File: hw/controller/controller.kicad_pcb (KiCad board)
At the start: 2 copper layers, 76.2 x 38.1 mm, 87 parts, among them J2 USB_OTG, J3 UART, P14 I2C0, P15 I2C1, P16 I2C2, P17 I2C3, P2 FRIDGE, P3 FAN, P4 PUMP, P5 MIST, SW1 RST, SW2 BOOT, U1 stm32f072x, U2 MIC550X, U3 tca9546a, U8 SHT3x-DIS, Y2 32768Hz

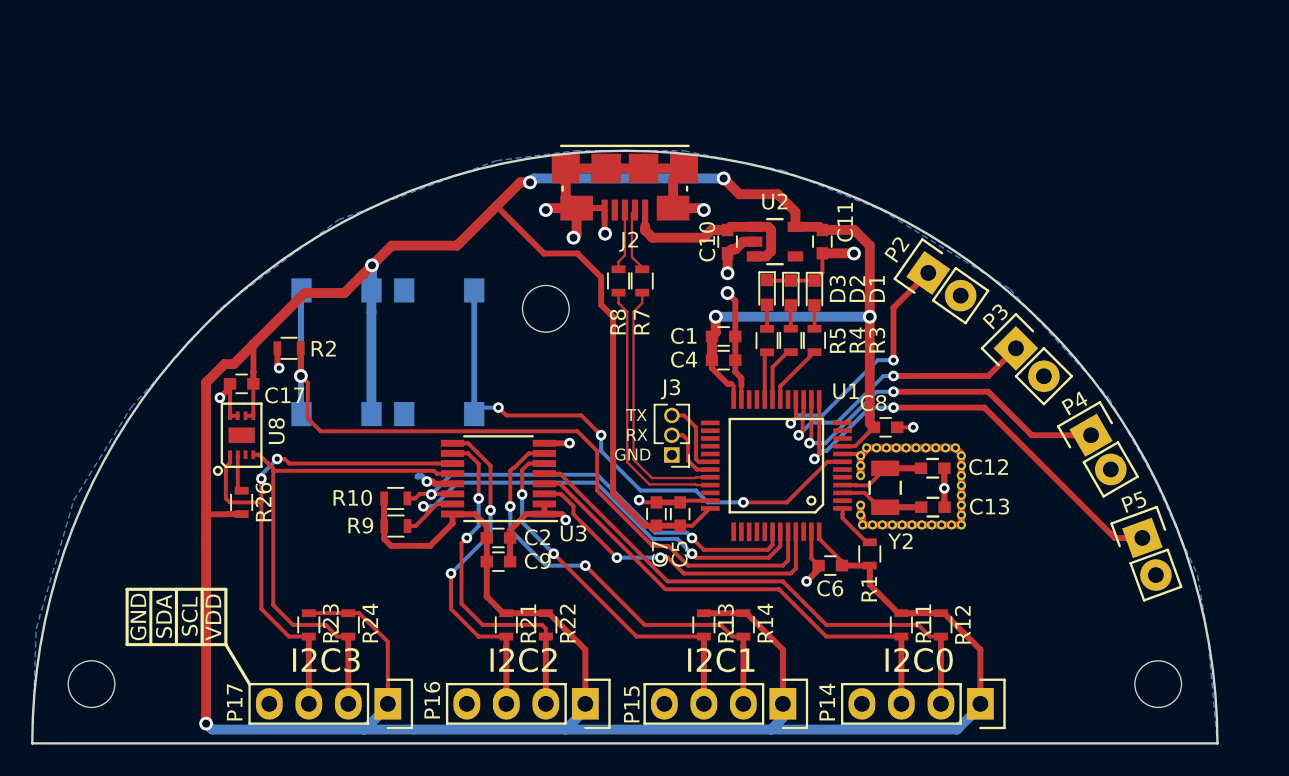
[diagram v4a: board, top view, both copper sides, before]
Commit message: Updated ostur_controller with NRF52810. Released v2.0
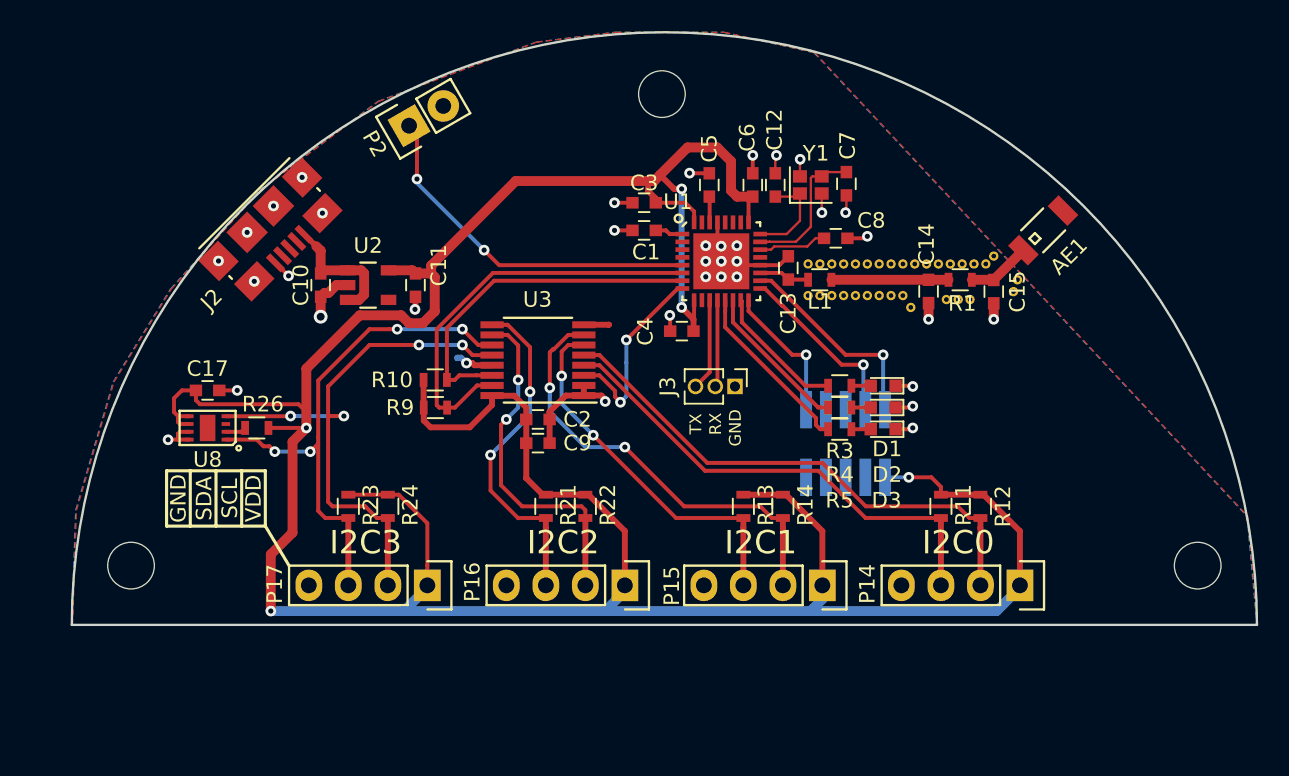
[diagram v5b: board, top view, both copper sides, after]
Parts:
- removed P3: FAN, Pin_Headers:Pin_Header_Straight_1x02
- removed P4: PUMP, Pin_Headers:Pin_Header_Straight_1x02
- removed P5: MIST, Pin_Headers:Pin_Header_Straight_1x02
- removed R2: 10k, Resistors_SMD:R_0603
- removed R7, R8: 22, Resistors_SMD:R_0603
- removed the REF** at (151.2, 96.0)
- removed the REF** at (155.8, 97.3)
- removed the REF** at (156.4, 97.3)
- removed the REF** at (157.1, 97.3)
- removed the REF** at (157.7, 97.3)
- removed the REF** at (157.7, 96.7)
- removed the REF** at (157.7, 96.0)
- removed the REF** at (157.7, 95.4)
- removed the REF** at (157.7, 94.8)
- removed the REF** at (157.7, 94.1)
- removed the REF** at (157.7, 93.5)
- removed the REF** at (151.2, 96.7)
- removed the REF** at (157.7, 92.9)
- removed the REF** at (157.3, 92.3)
- removed the REF** at (156.7, 92.3)
- removed the REF** at (156.0, 92.3)
- removed the REF** at (155.4, 92.3)
- removed the REF** at (154.8, 92.3)
- removed the REF** at (154.1, 92.3)
- removed the REF** at (153.5, 92.3)
- removed the REF** at (152.9, 92.3)
- removed the REF** at (151.6, 92.3)
- removed the REF** at (151.3, 97.3)
- removed the REF** at (151.2, 92.9)
- removed the REF** at (151.2, 93.5)
- removed the REF** at (151.2, 94.1)
- removed the REF** at (152.2, 92.3)
- removed the REF** at (152.0, 97.3)
- removed the REF** at (152.6, 97.3)
- removed the REF** at (153.2, 97.3)
- removed the REF** at (153.9, 97.3)
- removed the REF** at (154.5, 97.3)
- removed the REF** at (155.1, 97.3)
- removed SW1: RST, footprints:PTS645SM43SMTR92
- removed SW2: BOOT, footprints:PTS645SM43SMTR92
- removed Y2: 32768Hz, footprints:FC-135
- added AE1: Antenna, alvarop:AMCA31-2R450G-S1F-T3, F.Cu at (162.9, 78.4)
- added C14: DNP, Capacitors_SMD:C_0603, F.Cu at (155.6, 82.3)
- added C15: DNP, Capacitors_SMD:C_0603, F.Cu at (159.8, 82.3)
- added C3: 4.7uF, Capacitors_SMD:C_0603, F.Cu at (137.3, 76.6)
- added J1: ARM-SWD, alvarop:ARM_SWD_SMD, B.Cu at (150.2, 92.1)
- added L1: 3.9nH, Resistors_SMD:R_0603, F.Cu at (148.6, 81.5)
- added REF**: via-0.6mm, alvarop:via-0.6mm, F.Cu at (161.0, 82.3)
- added REF**: via-0.6mm, alvarop:via-0.6mm, F.Cu at (148.6, 82.5)
- added REF**: via-0.6mm, alvarop:via-0.6mm, F.Cu at (153.9, 82.5)
- added REF**: via-0.6mm, alvarop:via-0.6mm, F.Cu at (150.9, 82.5)
- added REF**: via-0.6mm, alvarop:via-0.6mm, F.Cu at (153.2, 82.5)
- added REF**: via-0.6mm, alvarop:via-0.6mm, F.Cu at (151.6, 82.5)
- added REF**: via-0.6mm, alvarop:via-0.6mm, F.Cu at (152.4, 82.5)
- added REF**: via-0.6mm, alvarop:via-0.6mm, F.Cu at (159.8, 80.0)
- added REF**: via-0.6mm, alvarop:via-0.6mm, F.Cu at (154.7, 80.5)
- added REF**: via-0.6mm, alvarop:via-0.6mm, F.Cu at (153.9, 80.5)
- added REF**: via-0.6mm, alvarop:via-0.6mm, F.Cu at (159.3, 80.5)
- added REF**: via-0.6mm, alvarop:via-0.6mm, F.Cu at (161.3, 81.5)
- added REF**: via-0.6mm, alvarop:via-0.6mm, F.Cu at (157.7, 80.5)
- added REF**: via-0.6mm, alvarop:via-0.6mm, F.Cu at (158.5, 80.5)
- added REF**: via-0.6mm, alvarop:via-0.6mm, F.Cu at (155.4, 80.5)
- added REF**: via-0.6mm, alvarop:via-0.6mm, F.Cu at (157.0, 80.5)
- added REF**: via-0.6mm, alvarop:via-0.6mm, F.Cu at (156.2, 80.5)
- added REF**: via-0.6mm, alvarop:via-0.6mm, F.Cu at (153.2, 80.5)
- added REF**: via-0.6mm, alvarop:via-0.6mm, F.Cu at (150.9, 80.5)
- added REF**: via-0.6mm, alvarop:via-0.6mm, F.Cu at (152.4, 80.5)
- added REF**: via-0.6mm, alvarop:via-0.6mm, F.Cu at (151.6, 80.5)
- added REF**: via-0.6mm, alvarop:via-0.6mm, F.Cu at (150.1, 80.5)
- added REF**: via-0.6mm, alvarop:via-0.6mm, F.Cu at (158.2, 82.8)
- added REF**: via-0.6mm, alvarop:via-0.6mm, F.Cu at (149.4, 80.5)
- added REF**: via-0.6mm, alvarop:via-0.6mm, F.Cu at (148.6, 80.5)
- added REF**: via-0.6mm, alvarop:via-0.6mm, F.Cu at (147.8, 80.5)
- added REF**: via-0.6mm, alvarop:via-0.6mm, F.Cu at (157.5, 82.8)
- added REF**: via-0.6mm, alvarop:via-0.6mm, F.Cu at (156.7, 82.8)
- added REF**: via-0.6mm, alvarop:via-0.6mm, F.Cu at (154.4, 83.3)
- added REF**: via-0.6mm, alvarop:via-0.6mm, F.Cu at (147.8, 82.5)
- added REF**: via-0.6mm, alvarop:via-0.6mm, F.Cu at (149.4, 82.5)
- added REF**: via-0.6mm, alvarop:via-0.6mm, F.Cu at (150.1, 82.5)
- added Y1: 32MHz, Crystals:Crystal_SMD_2016-4pin_2.0x1.6mm, F.Cu at (148.0, 75.4)
- C12: value 6pF -> 12pF
- C13: value 6pF -> 0.8pF
- C4: value 10nF -> 100nF
- C5: value 100nF -> 1uF
- C6: value 4.7uF -> 100nF
- C7: value 4.7uF -> 12pF
- C8: value 1uF -> 100pF
- U1: value stm32f072x -> NRF52810-QCAA; footprint footprints:LQFP48 -> NRF52810_QCAA_QFN32
- U8: footprint footprints:SHT3x -> SHT3x
- moved P2 34.7 mm to (122.2, 71.6), turned to 120 degrees
- moved C10 26.3 mm to (116.5, 81.9)
- moved C11 26.3 mm to (122.6, 81.9)
- moved U2 26.3 mm to (119.5, 81.9)
- moved C6 25.0 mm to (144.3, 75.4), turned to 90 degrees
- moved C7 24.5 mm to (150.3, 75.4), turned to 270 degrees
- moved J2 21.7 mm to (114.5, 79.5), turned to 225 degrees
- moved C5 21.2 mm to (141.5, 75.4)
- moved C12 20.8 mm to (145.7, 75.4), turned to 270 degrees
- moved R1 18.6 mm to (157.6, 81.5), turned to 0 degrees
- moved C13 18.0 mm to (146.6, 80.8), turned to 270 degrees
- moved REF** 15.7 mm to (138.4, 69.6)
- moved U1 13.6 mm to (142.2, 80.3), turned to 0 degrees
- moved C8 12.6 mm to (149.6, 78.9), turned to 180 degrees
- moved D3 11.5 mm to (152.7, 91.1), turned to 180 degrees
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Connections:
- C1 pad 1: VDD -> Net-(C1-Pad1)
- C12 pad 1: Net-(C12-Pad1) -> GND
- C12 pad 2: GND -> Net-(C12-Pad2)
- C13 pad 1: Net-(C13-Pad1) -> GND
- C13 pad 2: GND -> Net-(C13-Pad2)
- C5 pad 1: VDD -> Net-(C5-Pad1)
- C7 pad 1: VDD -> Net-(C7-Pad1)
- C8 pad 1: VDD -> GND
- C8 pad 2: GND -> Net-(C8-Pad2)
- J2 pad 2: /D_N -> Net-(J2-Pad2)
- J2 pad 3: /D_P -> Net-(J2-Pad3)
- R1 pad 1: VDD -> Net-(C14-Pad2)
- R1 pad 2: Net-(R1-Pad2) -> Net-(AE1-Pad1)
- U1 pad 1: Net-(R1-Pad2) -> Net-(C1-Pad1)
- U1 pad 11: Net-(U1-Pad11) -> /UART1_TX
- U1 pad 12: Net-(U1-Pad12) -> /UART1_RX
- U1 pad 13: /MIST -> /LED2
- U1 pad 14: /PUMP -> /LED1
- U1 pad 15: /FAN -> /LED0
- U1 pad 16: /FRIDGE -> /nRST
- U1 pad 17: Net-(U1-Pad17) -> /SWDCLK
- U1 pad 18: /LED0 -> /SWDIO
- U1 pad 19: /LED1 -> Net-(C13-Pad2)
- U1 pad 20: /LED2 -> GND
- U1 pad 22: Net-(U1-Pad22) -> Net-(C8-Pad2)
- U1 pad 23: GND -> Net-(C7-Pad1)
- U1 pad 24: VDD -> Net-(C12-Pad2)
- U1 pad 25: Net-(U1-Pad25) -> VDD
- U1 pad 29: Net-(U1-Pad29) -> GND
- U1 pad 3: Net-(C13-Pad1) -> Net-(U1-Pad3)
- U1 pad 30: /UART1_TX -> Net-(C5-Pad1)
- U1 pad 31: /UART1_RX -> Net-(U1-Pad31)
- U1 pad 32: /USB_N -> VDD
- U1 pad 4: Net-(C12-Pad1) -> Net-(U1-Pad4)
- U1 pad 5: Net-(U1-Pad5) -> /FRIDGE
- U1 pad 6: Net-(U1-Pad6) -> /SDA
- U1 pad 7: /nRST -> /SCL
- U1 pad 8: GND -> /TCA_nRST
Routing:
- net VDD: track 271.5 -> 210.9 mm, vias 6 -> 5
- net /boot0: track 50.9 -> 0.00 mm, vias 1 -> 0
- net GND: track 90.4 -> 43.0 mm, vias 16 -> 37
- net /MIST: track 29.9 -> 0.00 mm, vias 2 -> 0
- net /nRST: track 36.0 -> 9.09 mm, vias 3 -> 1
- net /PUMP: track 23.5 -> 0.00 mm, vias 2 -> 0
- net /FAN: track 18.7 -> 0.00 mm, vias 2 -> 0
- net /USB_P: track 17.1 -> 0.00 mm
- net /USB_N: track 16.4 -> 0.00 mm
- net /SWDIO: track 0.00 -> 13.5 mm, vias 0 -> 1
- net /SWDCLK: track 0.00 -> 11.6 mm, vias 0 -> 1
- net Net-(C7-Pad1): track 0.00 -> 9.24 mm
- net /TCA_nRST: track 21.1 -> 12.4 mm
- net /LED2: track 3.10 -> 11.3 mm
- net Net-(C14-Pad2): track 0.00 -> 7.53 mm
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- added copper zone on F.Cu, net GND
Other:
- rule pad_to_mask_clearance: 0.1016 -> 0.0508
- board text added: "Controller v2.0"
- board text removed: "Controller v1.4"
- board text removed: "dfu"
- board text removed: "rst"

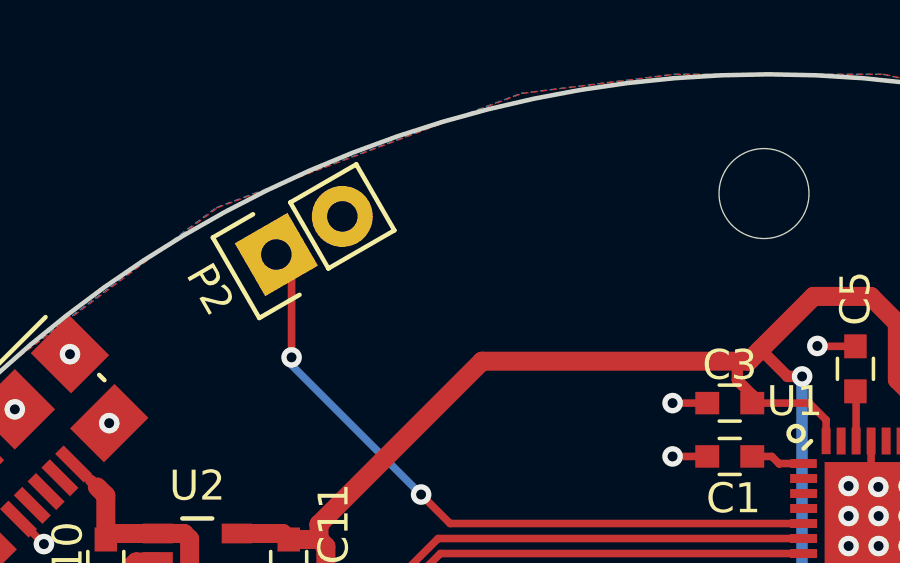
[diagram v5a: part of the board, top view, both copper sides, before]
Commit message: Updating BOM and silkscreen fixes for controller 2.0
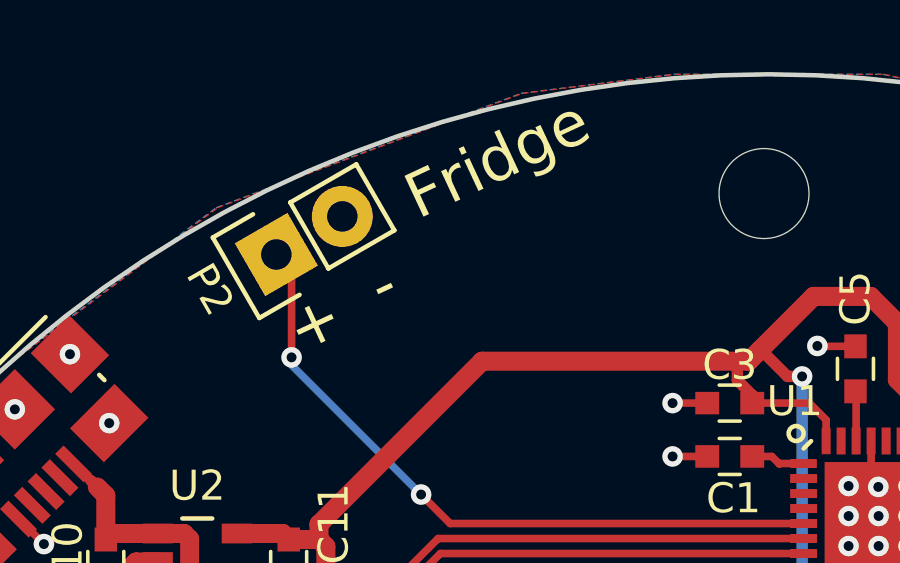
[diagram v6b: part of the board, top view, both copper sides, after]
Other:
- board text added: "+"
- board text added: "-"
- board text added: "Fridge"
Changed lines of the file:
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@@
     (links 167)
     (no_connects 0)
-    (area 79.982287 61.228554 178.906868 114.587)
+    (area 100.413207 65.546029 176.763209 103.796031)
     (thickness 1.6)
-    (drawings 27)
+    (drawings 30)
     (tracks 462)
     (zones 0)
@@
   )
   (setup
-    (last_trace_width 0.254)
+    (last_trace_width 0.1524)
     (user_trace_width 0.1524)
     (user_trace_width 0.254)
@@
     (pad "" smd rect (at 0 1.8 135) (size 1.8 1) (layers F.Cu F.Paste F.Mask))
   )
+  (gr_text - (at 125.73 72.644 25) (layer F.SilkS)
+    (effects (font (size 1.5 1.5) (thickness 0.25)))
+  )
+  (gr_text + (at 123.444 73.914 25) (layer F.SilkS)
+    (effects (font (size 1.5 1.5) (thickness 0.25)))
+  )
+  (gr_text Fridge (at 129.54 68.453 25) (layer F.SilkS)
+    (effects (font (size 1.5 1.5) (thickness 0.25)))
+  )
   (dimension 76.2 (width 0.3) (layer F.Fab)
     (gr_text "3.0000 in" (at 138.557 113.236999) (layer F.Fab)
@@
     (arrow2b (pts (xy 86.868 65.532) (xy 87.454421 66.658504)))
   )
-  (gr_text Ostur (at 146.304 78.486) (layer B.SilkS)
+  (gr_text Ostur (at 139.319 77.978) (layer B.SilkS)
     (effects (font (size 7 7) (thickness 1.5)) (justify mirror))
   )
-  (gr_text "Controller v2.0" (at 142.748 85.852) (layer B.SilkS)
+  (gr_text "Controller v2.0" (at 135.128 85.725) (layer B.SilkS)
     (effects (font (size 3 3) (thickness 0.75)) (justify mirror))
   )
@@
   (gr_arc (start 138.588208 103.72103) (end 100.488208 103.72103) (angle 180) (layer Edge.Cuts) (width 0.15))
   (gr_line (start 100.488208 103.72103) (end 176.688208 103.72103) (layer Edge.Cuts) (width 0.15))
-  (gr_text "by  @alvaroprieto" (at 132.334 91.186) (layer B.SilkS)
+  (gr_text "by  @alvaroprieto" (at 132.08 92.075) (layer B.SilkS)
     (effects (font (size 2 2) (thickness 0.3)) (justify mirror))
   )

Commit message: Released Ostur Controller v2.1
NOTE: Used kicad 5
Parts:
- removed J3: UART, Pin_Headers:Pin_Header_Straight_1x03_Pitch1.27mm
- added C16: 100nF, Capacitor_SMD:C_0603_1608Metric, F.Cu at (121.4, 75.7)
- added C18: 10nF, Capacitor_SMD:C_0603_1608Metric, F.Cu at (119.9, 75.7)
- added L2: FB, Resistor_SMD:R_0603_1608Metric, F.Cu at (120.7, 78.0)
- added R2: 27, Resistor_SMD:R_0603_1608Metric, F.Cu at (119.6, 82.3)
- added R6: 27, Resistor_SMD:R_0603_1608Metric, F.Cu at (119.6, 80.3)
- added U4: FT234XD, alvarop:FTDI_DFN12, F.Cu at (123.2, 81.3)
- moved C10 15.7 mm to (129.7, 73.3)
- moved U2 15.5 mm to (132.8, 73.8), turned to 0 degrees
- moved C11 11.3 mm to (132.8, 76.9), turned to 180 degrees
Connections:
- J2 pad 1: +5V -> /VDD_5
- J2 pad 2: Net-(J2-Pad2) -> /USB_DM
- J2 pad 3: Net-(J2-Pad3) -> /USB_DP
- U1 pad 11: /UART1_TX -> Net-(U1-Pad11)
- U1 pad 12: /UART1_RX -> Net-(U1-Pad12)
- U1 pad 3: Net-(U1-Pad3) -> /UART1_TX
- U1 pad 4: Net-(U1-Pad4) -> /UART1_RX
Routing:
- net /UART1_TX: track 5.92 -> 19.1 mm
- net /UART1_RX: track 5.61 -> 16.3 mm
- net +5V: track 8.50 -> 17.8 mm
- net VDD: track 210.9 -> 217.7 mm, vias 5 -> 7
- net /VDD_5: track 0.00 -> 6.78 mm
- net /USB_DM: track 0.00 -> 5.22 mm
- net /USB_DP: track 0.00 -> 4.89 mm, vias 0 -> 2
- net Net-(R2-Pad2): track 0.00 -> 1.86 mm
- net Net-(R6-Pad1): track 0.00 -> 1.86 mm
- net GND: track 43.0 -> 42.0 mm, vias 37 -> 39
- net /FRIDGE: track 23.1 -> 23.4 mm, vias 2 -> 1
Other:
- board text added: "Controller v2.1"
- board text removed: "Controller v2.0"
